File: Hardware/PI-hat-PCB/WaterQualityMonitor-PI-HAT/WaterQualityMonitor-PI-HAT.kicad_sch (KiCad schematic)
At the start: 7 parts

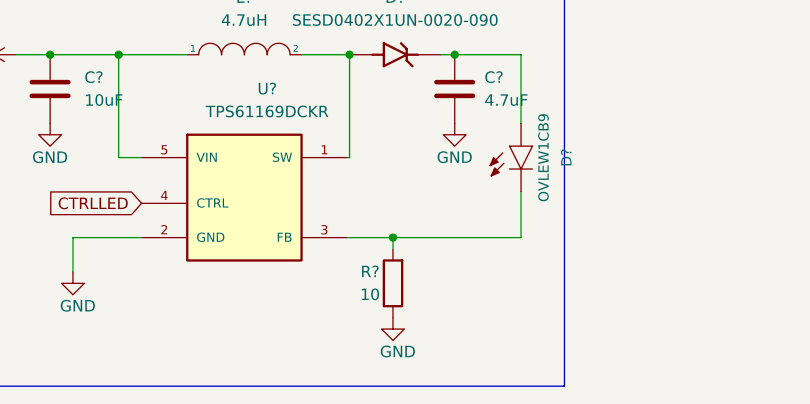
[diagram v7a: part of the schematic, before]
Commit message: changed current sense resistor value to deliver 40 ma
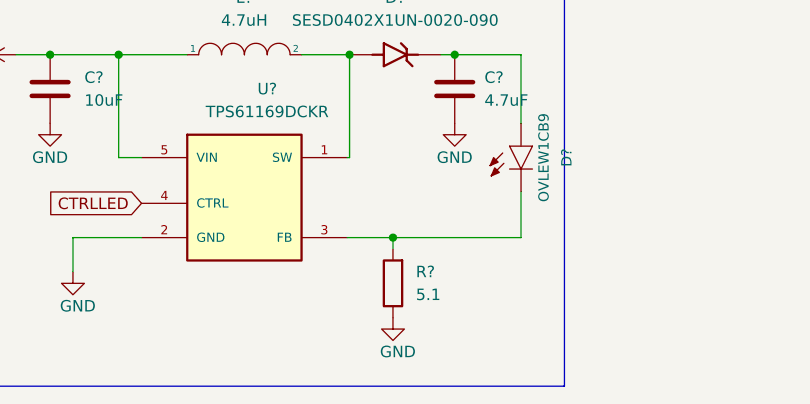
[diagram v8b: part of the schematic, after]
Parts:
- R?: value 10 -> 5.1
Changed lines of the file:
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@@
   (symbol (lib_id "Device:R") (at 63.5 49.53 180) (unit 1)
     (in_bom yes) (on_board yes) (fields_autoplaced)
-    (property "Reference" "R?" (id 0) (at 60.96 48.26 0))
-    (property "Value" "10" (id 1) (at 60.96 50.8 0))
+    (property "Reference" "R?" (id 0) (at 66.04 48.2599 0)
+      (effects (font (size 1.27 1.27)) (justify right))
+    )
+    (property "Value" "5.1" (id 1) (at 66.04 50.7999 0)
+      (effects (font (size 1.27 1.27)) (justify right))
+    )
     (property "Footprint" "" (id 2) (at 65.278 49.53 90)
       (effects (font (size 1.27 1.27)) hide)
@@
     )
     (path "/6b423158-56f2-4aac-bab7-adb690d7dca0"
-      (reference "R?") (unit 1) (value "10") (footprint "")
+      (reference "R?") (unit 1) (value "5.1") (footprint "")
     )
     (path "/42f59bf4-af48-4db1-8bdf-07de8825d459/91536648-8bec-4010-8981-2ab46b350c0b"
